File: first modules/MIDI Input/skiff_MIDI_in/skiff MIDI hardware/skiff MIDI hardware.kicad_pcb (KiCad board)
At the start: 2 copper layers, 13 parts, among them J2 AudioJack3, U1 H11L1

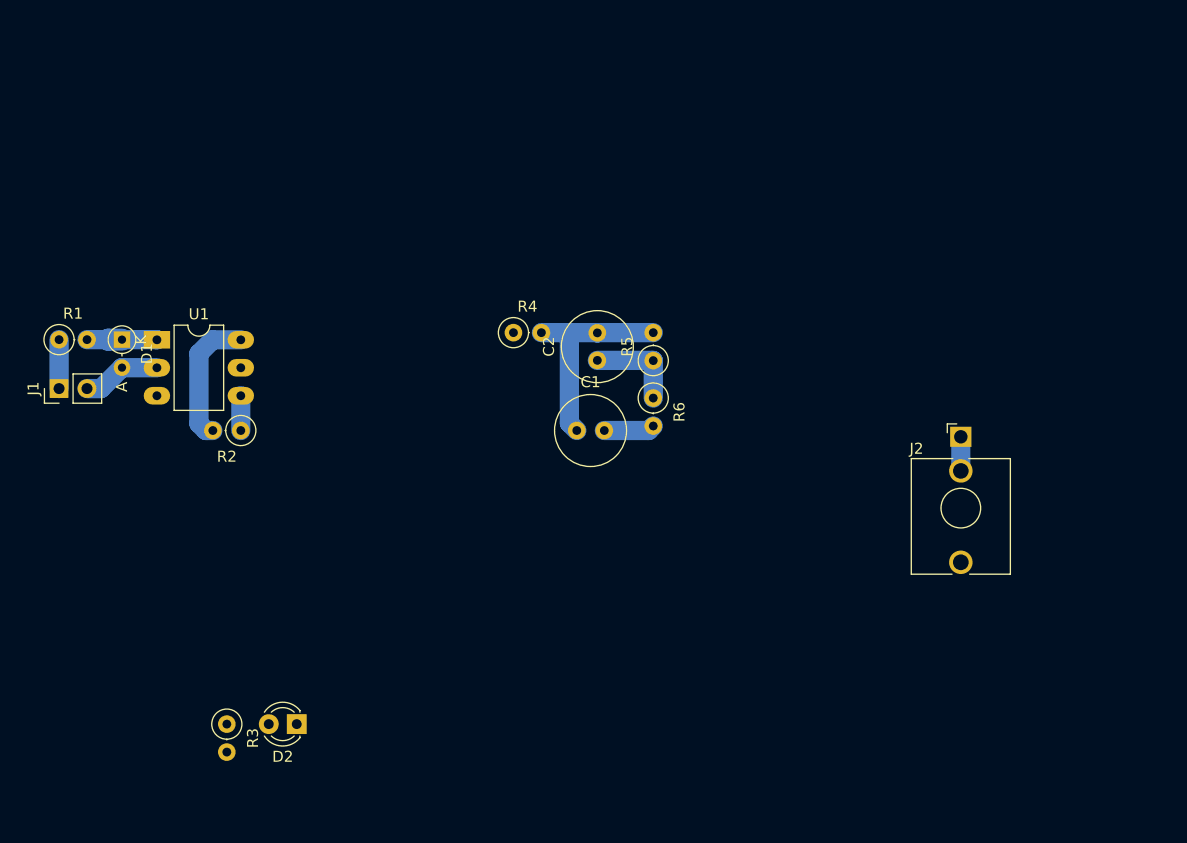
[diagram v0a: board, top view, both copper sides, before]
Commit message: PCB in progress; Schematic lacks only output stages (Outputs don't yet conform to Modular Synth signal standards, but schematic should be otherwise ok.)
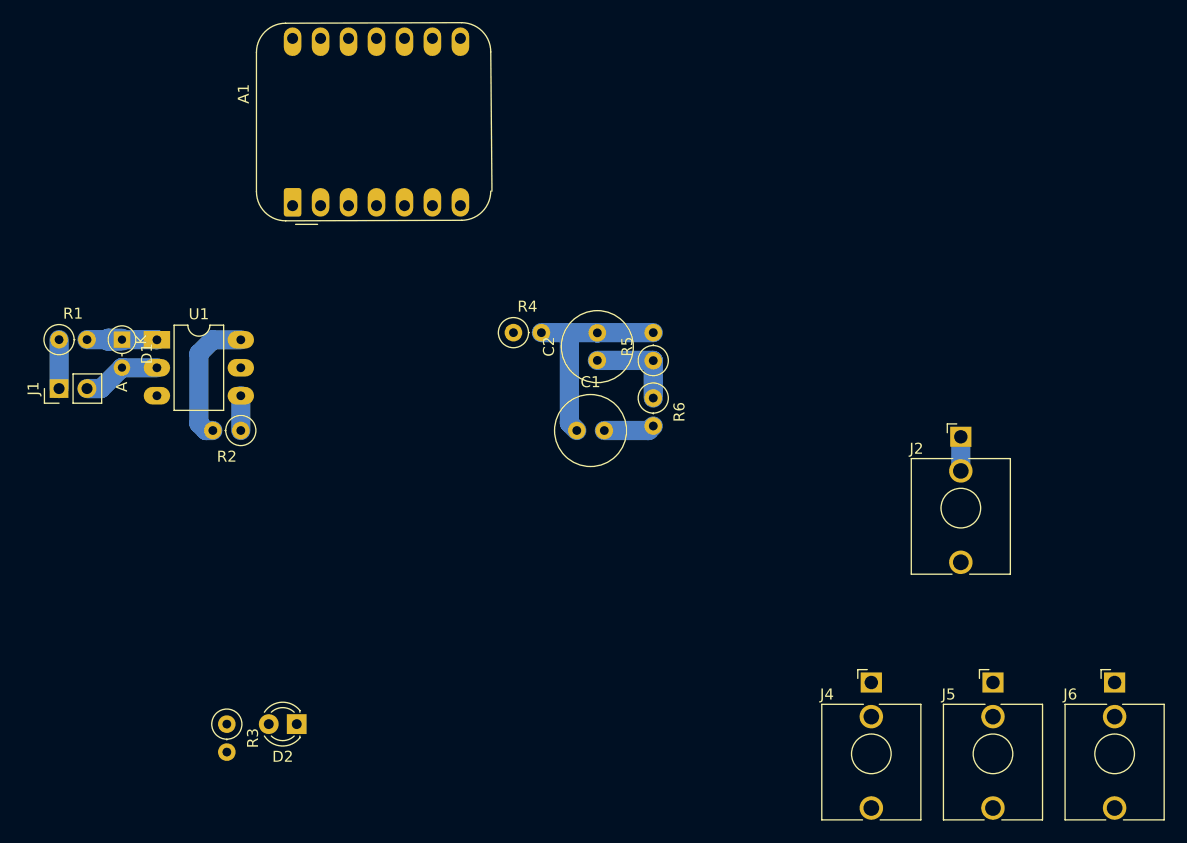
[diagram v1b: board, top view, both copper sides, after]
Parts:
- added A1: Adafruit_QT_PY_RP2040_DSE, DSE_Custom_Footprints:Adafruit_QT_PY_RP2040_DSE, F.Cu at (58.0, 48.8)
- added J4: CV Out, Connector_Audio:Jack_3.5mm_QingPu_WQP-PJ398SM_Vertical_CircularHoles, F.Cu at (107.4, 92.1)
- added J5: Gate Out, Connector_Audio:Jack_3.5mm_QingPu_WQP-PJ398SM_Vertical_CircularHoles, F.Cu at (118.5, 92.1)
- added J6: Clock Out, Connector_Audio:Jack_3.5mm_QingPu_WQP-PJ398SM_Vertical_CircularHoles, F.Cu at (129.5, 92.1)
- J2: value AudioJack3 -> Audio Out
